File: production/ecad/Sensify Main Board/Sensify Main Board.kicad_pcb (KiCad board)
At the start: 4 copper layers, 31.8 x 130 mm, 139 parts, among them J1 1-2834011-3, J2 1-2834011-2, J3 1332645, J4 0532611271, J6 Conn_01x02_Socket, J7 Conn_01x02_Socket, J8 Conn_01x02_Socket, J9 Conn_01x02_Socket, Q1 2N700, Q2 PMPB13XNE,115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

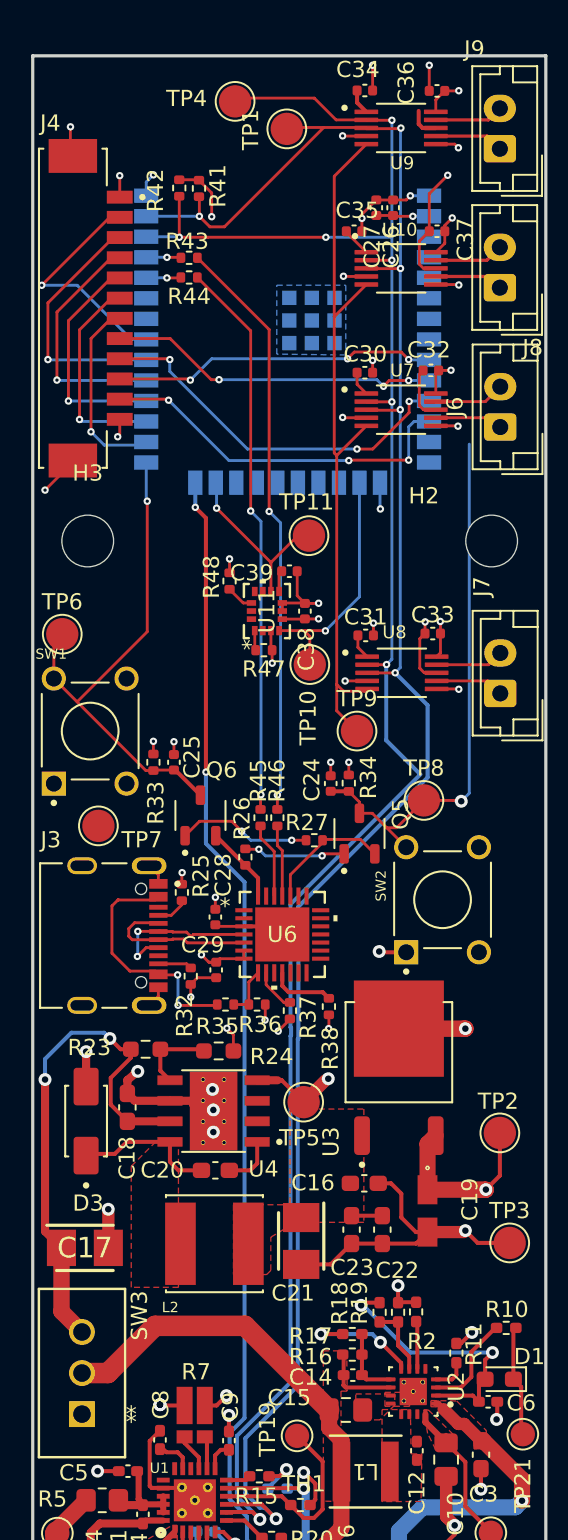
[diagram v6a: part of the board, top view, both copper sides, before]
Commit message: Under 6 No Connections, less than 100 DRC errors...
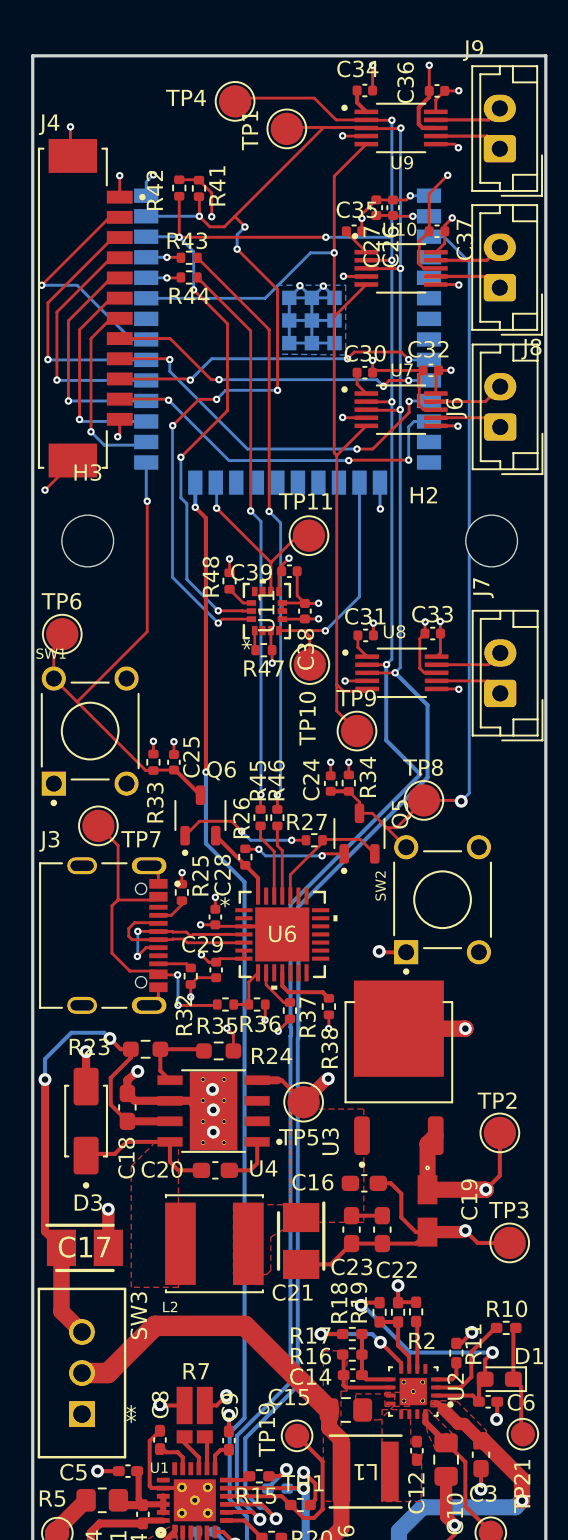
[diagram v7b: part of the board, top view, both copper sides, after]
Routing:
- net SDA: track 124.3 -> 159.5 mm, vias 6 -> 12
- net SCL: track 127.7 -> 156.2 mm, vias 7 -> 10
- net GND: track 160.9 -> 187.4 mm, vias 49 -> 52
- net EN: track 34.6 -> 49.0 mm
- net HAPTICS_EN: track 45.2 -> 58.0 mm, vias 0 -> 1
- net FLASHING_VBUS_5V: track 15.0 -> 20.1 mm
- net +3V3: track 37.3 -> 38.3 mm, vias 13 -> 14

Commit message: Down to 32 DRC Errors
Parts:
- moved TP20 3.48 mm to (157.9, 156.1)
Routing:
- net Net-(U2-PMID): track 9.96 -> 13.2 mm
- net EN: track 49.0 -> 50.9 mm
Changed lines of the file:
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@@
   )
   (footprint "TestPoint:TestPoint_Pad_D1.5mm" (layer "F.Cu")
-    (at 155.8544 153.2636 180)
+    (at 157.8864 156.083 180)
     (descr "SMD pad as test Point, diameter 1.5mm")
     (tags "test point SMD pad")
@@
     (pts (xy 159.258 61.8744) (xy 159.258 91.8972))
     (height -6.0452)
-    (gr_text "1.1820 in" (at 163.5032 76.8858 90) (layer "F.Cu")
+    (gr_text "30.0228 mm" (at 163.5032 76.8858 90) (layer "F.Cu")
       (effects (font (size 1.5 1.5) (thickness 0.3)))
     )
@@
   (segment (start 138.791 148.483) (end 139.1412 148.1328) (width 0.25) (layer "F.Cu") (net 14))
   (segment (start 151.8063 146.419) (end 153.0883 147.701) (width 0.381) (layer "F.Cu") (net 15))
-  (segment (start 154.2796 151.638) (end 156.21 153.5684) (width 0.25) (layer "F.Cu") (net 15))
+  (segment (start 154.2796 148.8923) (end 154.2796 152.4762) (width 0.25) (layer "F.Cu") (net 15))
   (segment (start 151.8063 145.926) (end 151.8063 146.419) (width 0.381) (layer "F.Cu") (net 15))
   (segment (start 153.0883 147.701) (end 154.2796 148.8923) (width 0.25) (layer "F.Cu") (net 15))
-  (segment (start 154.2796 148.8923) (end 154.2796 151.638) (width 0.25) (layer "F.Cu") (net 15))
+  (segment (start 154.2796 152.4762) (end 157.8864 156.083) (width 0.25) (layer "F.Cu") (net 15))
   (segment (start 153.0883 147.701) (end 153.0883 147.208) (width 0.25) (layer "F.Cu") (net 15))
   (segment (start 138.791 153.212) (end 139.293 153.212) (width 0.25) (layer "F.Cu") (net 16))
@@
   (segment (start 145.9484 107.384) (end 147.0588 107.384) (width 0.25) (layer "F.Cu") (net 25))
   (via (at 154.0256 108.0008) (size 0.8) (drill 0.4) (layers "F.Cu" "B.Cu") (net 25))
-  (segment (start 152.9585 73.0704) (end 152.0314 73.0704) (width 0.1778) (layer "B.Cu") (net 25))
-  (segment (start 154.0256 108.0008) (end 154.519097 107.507303) (width 0.1778) (layer "B.Cu") (net 25))
-  (segment (start 154.519097 107.507303) (end 154.519097 74.630997) (width 0.1778) (layer "B.Cu") (net 25))
+  (segment (start 154.519097 88.406503) (end 154.519097 88.0364) (width 0.1778) (layer "B.Cu") (net 25))
+  (segment (start 154.519097 88.0364) (end 154.519097 74.630997) (width 0.1778) (layer "B.Cu") (net 25))
   (segment (start 154.519097 74.630997) (end 152.9585 73.0704) (width 0.1778) (layer "B.Cu") (net 25))
+  (segment (start 152.2222 95.0976) (end 152.2222 90.7034) (width 0.1778) (layer "B.Cu") (net 25))
+  (segment (start 154.0256 108.0008) (end 154.519097 107.507303) (width 0.1778) (layer "B.Cu") (net 25))
+  (segment (start 154.519097 97.394497) (end 152.2222 95.0976) (width 0.1778) (layer "B.Cu") (net 25))
+  (segment (start 152.9585 73.0704) (end 152.0314 73.0704) (width 0.1778) (layer "B.Cu") (net 25))
+  (segment (start 152.2222 90.7034) (end 154.519097 88.406503) (width 0.1778) (layer "B.Cu") (net 25))
+  (segment (start 154.519097 107.507303) (end 154.519097 97.394497) (width 0.1778) (layer "B.Cu") (net 25))
   (segment (start 130.2553 101.8499) (end 134.5946 97.5106) (width 0.1778) (layer "F.Cu") (net 26))
   (segment (start 134.5946 97.5106) (end 134.5946 89.4334) (width 0.1778) (layer "F.Cu") (net 26))
@@
   (segment (start 136.138601 116.0609) (end 136.174701 116.097) (width 0.1778) (layer "F.Cu") (net 82))
   (segment (start 135.2836 116.0609) (end 136.138601 116.0609) (width 0.1778) (layer "F.Cu") (net 82))
-  (segment (start 135.338 116.0065) (end 135.2836 116.0609) (width 0.1778) (layer "F.Cu") (net 82))
   (segment (start 134.0104 116.0526) (end 135.2753 116.0526) (width 0.1778) (layer "F.Cu") (net 82))
   (segment (start 137.4521 116.2431) (end 140.5763 116.2431) (width 0.1778) (layer "F.Cu") (net 82))
